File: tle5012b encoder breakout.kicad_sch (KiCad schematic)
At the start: 12 parts, among them J1 Conn_01x02, J2 Conn_01x06, J3 Conn_01x06, U1 TLE5012

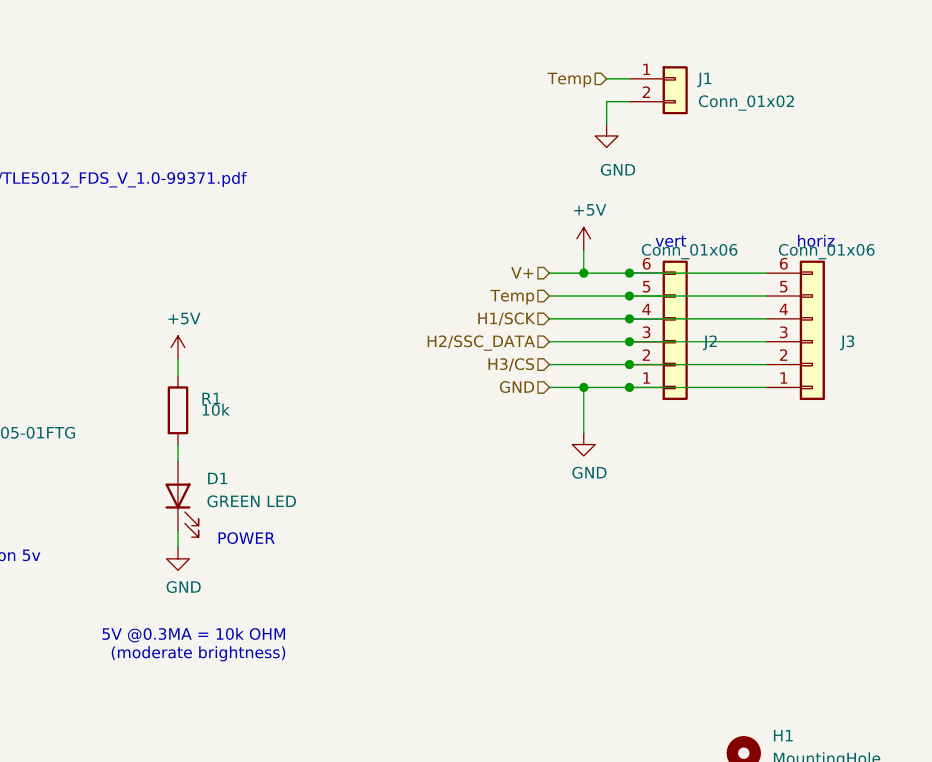
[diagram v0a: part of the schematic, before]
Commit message: Connected connector mounting pads to gnd plane for structural support
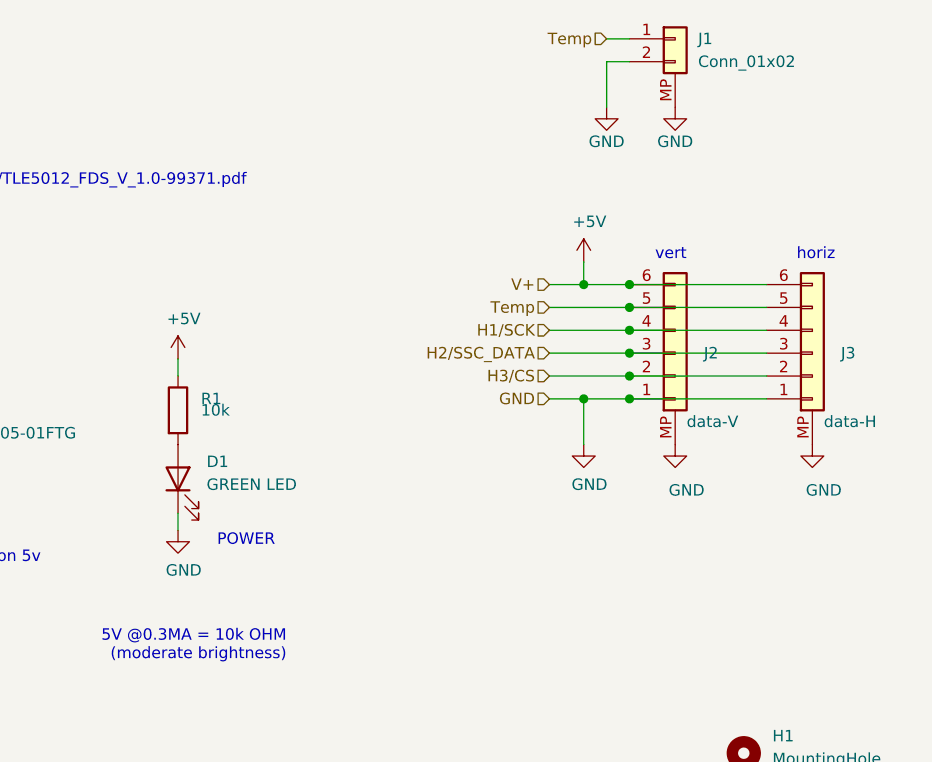
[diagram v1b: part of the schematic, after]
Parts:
- J2: value Conn_01x06 -> data-V
- J3: value Conn_01x06 -> data-H
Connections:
- net GND: now also J1.MP, J2.MP, J3.MP
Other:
- moved on the sheet: D1
